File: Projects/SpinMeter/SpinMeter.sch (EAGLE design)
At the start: 4 parts, among them IC1 LIS2DW12TR, IC2 BMD-340-A-R, U1 BMG250, U2 FDC1004DSCT

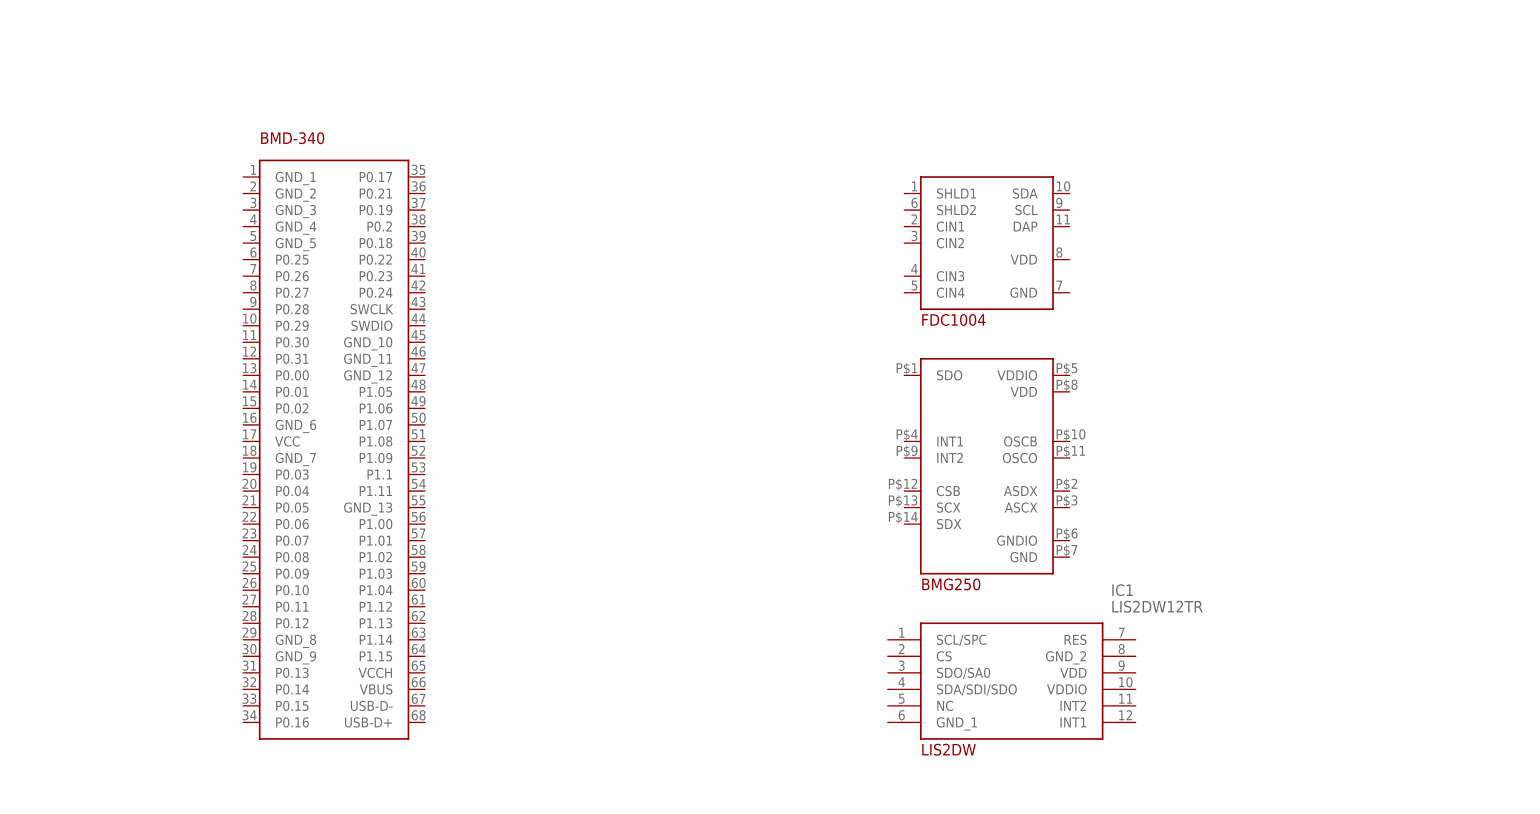
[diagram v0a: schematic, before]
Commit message: New libraries Board routing started
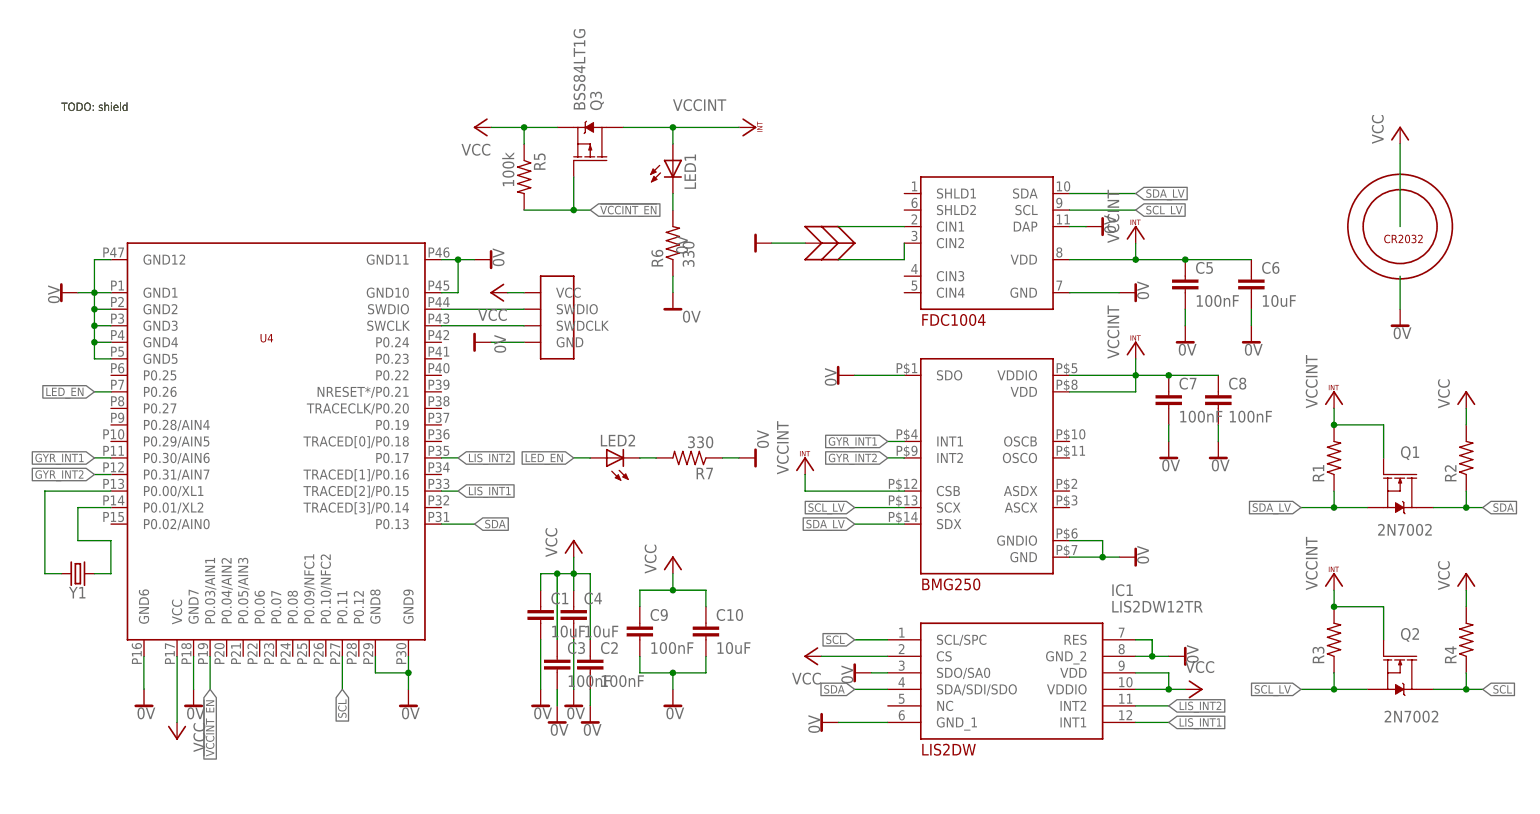
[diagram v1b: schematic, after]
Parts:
- removed IC2: BMD-340-A-R, Rigado:BMD-340-A-R
- added C1, C10, C4, C6: 10uF, rcl:C-EUC0603
- added C2, C3, C5, C7, C8, C9: 100nF, rcl:C-EUC0603
- added LED1, LED2: (no value), adafruit:LEDCHIP-LED0603
- added Q1, Q2: 2N7002, MOSFETS:2N7002
- added Q3: BSS84LT1G, MOSFETS:BSS84LT1G
- added R1, R2, R3, R4: (no value), rcl:R-US_R0603
- added R5: 100k, rcl:R-US_R0603
- added R6, R7: 330, rcl:R-US_R0603
- added U$1: PROG_SMD, Prog:PROG_SMD
- added U$2: IDC_SHEAR, IDC:IDC_SHEAR
- added U3: BAT-HLD-001-THM, BatteryHolder:BAT-HLD-001-THM
- added U4: (no value), Rigado:BMD-300
- added Y1: (no value), Sparkfun-clocks:CRYSTALSMD-3.2X1.5
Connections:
- new net !VCCINT_EN: Q3.G, R5.2, U4.P0.03/AIN1
- new net 0V: C1.2, C10.2, C2.2, C3.2, C4.2, C5.2, C6.2, C7.2, C8.2, C9.2, IC1.GND_1, IC1.GND_2, IC1.RES, IC1.SDO/SA0, R6.1, R7.1, U$1.GND, U$2.P$1, U1.GND, U1.GNDIO, U1.SDO, U2.DAP, U2.GND, U3.-, U4.GND1, U4.GND10, U4.GND11, U4.GND12, U4.GND2, U4.GND3, U4.GND4, U4.GND5, U4.GND6, U4.GND7, U4.GND8, U4.GND9
- new net GYR_INT1: U1.INT1, U4.P0.30/AIN6
- new net GYR_INT2: U1.INT2, U4.P0.31/AIN7
- new net LED_EN: LED2.A, U4.P0.26
- new net LIS_INT1: IC1.INT1, U4.TRACED[2]/P0.15
- new net LIS_INT2: IC1.INT2, U4.P0.17
- new net N$1: U$2.P$2, U2.CIN1
- new net N$2: U$2.P$3, U2.CIN2
- new net N$3: U$1.SWDIO, U4.SWDIO
- new net N$4: U$1.SWDCLK, U4.SWCLK
- new net N$5: LED1.C, R6.2
- new net N$6: LED2.C, R7.2
- new net N$7: U4.P0.00/XL1, Y1.2
- new net N$8: U4.P0.01/XL2, Y1.1
- new net SCL: IC1.SCL/SPC, Q2.D, R4.1, U4.P0.11
- new net SCL_LV: Q2.S, R3.1, U1.SCX, U2.SCL
- new net SDA: IC1.SDA/SDI/SDO, Q1.D, R2.1, U4.P0.13
- new net SDA_LV: Q1.S, R1.1, U1.SDX, U2.SDA
- new net VCC: C1.1, C10.1, C2.1, C3.1, C4.1, C9.1, IC1.CS, IC1.VDD, IC1.VDDIO, Q3.S, R2.2, R4.2, R5.1, U$1.VCC, U3.+, U4.VCC
- new net VCCINT: C5.1, C6.1, C7.1, C8.1, LED1.A, Q1.G, Q2.G, Q3.D, R1.2, R3.2, U1.CSB, U1.VDD, U1.VDDIO, U2.VDD
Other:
- note added: "TODO: shield"

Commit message: Finished board
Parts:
- removed Q3: BSS84LT1G, MOSFETS:BSS84LT1G
- added D1: BAT54H, Diodes:BAT54H
- added R8: (no value), rcl:R-US_R0201
- added R9: 100k, rcl:R-US_R0603
- added T2: BSS84, nxp_60:BSS84
- added U$10: SKRMAAE010, Buttons:SKRMAAE010
- added U$3: IDC_SHIELD, IDC:IDC_SHIELD
- added U$4: 36003250S, Shields:36003250S
- added U$5, U$6, U$7, U$8: TESTPOINT_22, test_points:TESTPOINT_22
- added U$9: TPS7A0531PDBVR, PowerSupplies:TPS7A05XX
- R1, R2, R3, R4: value (none) -> 22k
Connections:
- new net BTN: U$10.P$1, U4.P0.25
- new net HV_EN: U$9.EN, U4.TRACECLK/P0.20
- new net N$10: R8.1, U2.SHLD1
- new net N$9: R5.1, R9.1, T2.G
- new net SHIELD: R8.2, U$3.P$1, U$4.P$1
- new net VDD: C1.1, D1.A, U$9.IN, U3.+
- net !VCCINT_EN: now also R9.2, U4.P0.19; no longer Q3.G, R5.2, U4.P0.03/AIN1
- net 0V: now also U$10.P$2, U$5.P$1, U$9.GND
- net SCL_LV: now also U$7.P$1
- net SDA_LV: now also U$6.P$1
- net VCC: now also D1.K, R5.2, T2.S, U$9.OUT; no longer C1.1, Q3.S, R5.1, U3.+
- net VCCINT: now also T2.D, U$8.P$1; no longer Q3.D
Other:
- note removed: "TODO: shield"
- moved on the sheet: LED1, R5, R6

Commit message: Massive library update Added projects Added 3D packages
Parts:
- removed C5: 100nF, rcl:C-EUC0603
- removed C6: 10uF, rcl:C-EUC0603
- removed D1: BAT54H, Diodes:BAT54H
- removed LED1: (no value), adafruit:LEDCHIP-LED0603
- removed Q1, Q2: 2N7002, MOSFETS:2N7002
- removed R1, R3: 22k, rcl:R-US_R0603
- removed R5, R9: 100k, rcl:R-US_R0603
- removed R6: 330, rcl:R-US_R0603
- removed R8: (no value), rcl:R-US_R0201
- removed T2: BSS84, nxp_60:BSS84
- removed U$3: IDC_SHIELD, IDC:IDC_SHIELD
- removed U$4: 36003250S, Shields:36003250S
- removed U$6, U$7, U$8: TESTPOINT_22, test_points:TESTPOINT_22
- removed U$9: TPS7A0531PDBVR, PowerSupplies:TPS7A05XX
- removed U2: FDC1004DSCT, ADC:FDC1004DSCT
- U$2: value IDC_SHEAR -> TESTPOINT_22; device IDC:IDC_SHEAR -> test_points:TESTPOINT_22
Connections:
- removed net !VCCINT_EN: R9.2, U4.P0.19
- removed net HV_EN: U$9.EN, U4.TRACECLK/P0.20
- removed net N$1: U$2.P$2, U2.CIN1
- removed net N$10: R8.1, U2.SHLD1
- removed net N$2: U$2.P$3, U2.CIN2
- removed net N$5: LED1.C, R6.2
- removed net N$9: R5.1, R9.1, T2.G
- removed net SCL_LV: Q2.S, R3.1, U$7.P$1, U1.SCX, U2.SCL
- removed net SDA_LV: Q1.S, R1.1, U$6.P$1, U1.SDX, U2.SDA
- removed net SHIELD: R8.2, U$3.P$1, U$4.P$1
- removed net VCCINT: C5.1, C6.1, C7.1, C8.1, LED1.A, Q1.G, Q2.G, R1.2, R3.2, T2.D, U$8.P$1, U1.CSB, U1.VDD, U1.VDDIO, U2.VDD
- removed net VDD: C1.1, D1.A, U$9.IN, U3.+
- net 0V: no longer C5.2, C6.2, R6.1, U$2.P$1, U$9.GND, U2.DAP, U2.GND
- net GYR_INT1: now also U4.P0.08; no longer U4.P0.30/AIN6
- net GYR_INT2: now also U4.P0.10/NFC2; no longer U4.P0.31/AIN7
- net SCL: now also U1.SCX; no longer Q2.D
- net SDA: now also U1.SDX; no longer Q1.D
- net VCC: now also C1.1, C7.1, C8.1, U$2.P$1, U1.CSB, U1.VDD, U1.VDDIO, U3.+; no longer D1.K, R5.2, T2.S, U$9.OUT
